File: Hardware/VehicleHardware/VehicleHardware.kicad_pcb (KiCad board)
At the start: 2 copper layers, 157.5 x 45.7 mm, 12 parts, among them U1 LM7805_TO220, U2 ESP32-CAM, U3 L298HN

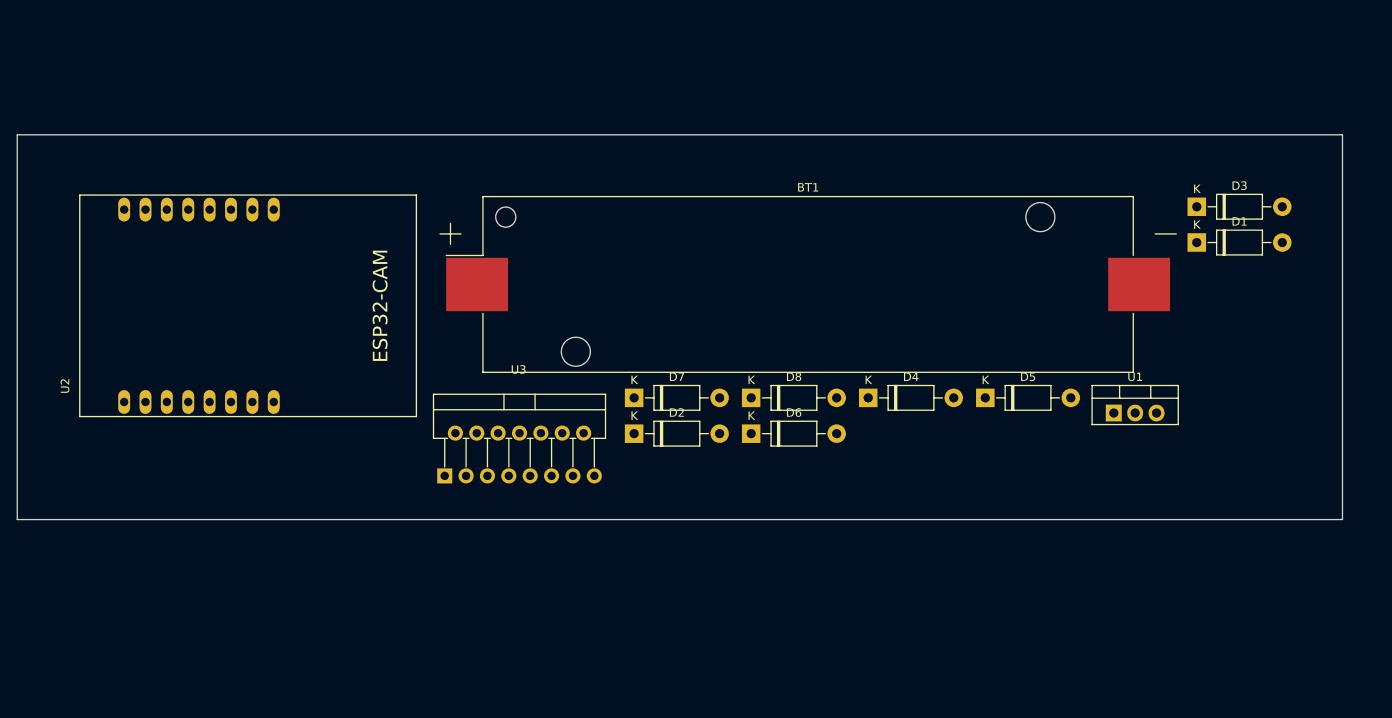
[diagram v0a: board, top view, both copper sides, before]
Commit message: added esp32-cam 3d-model; updated pcb design
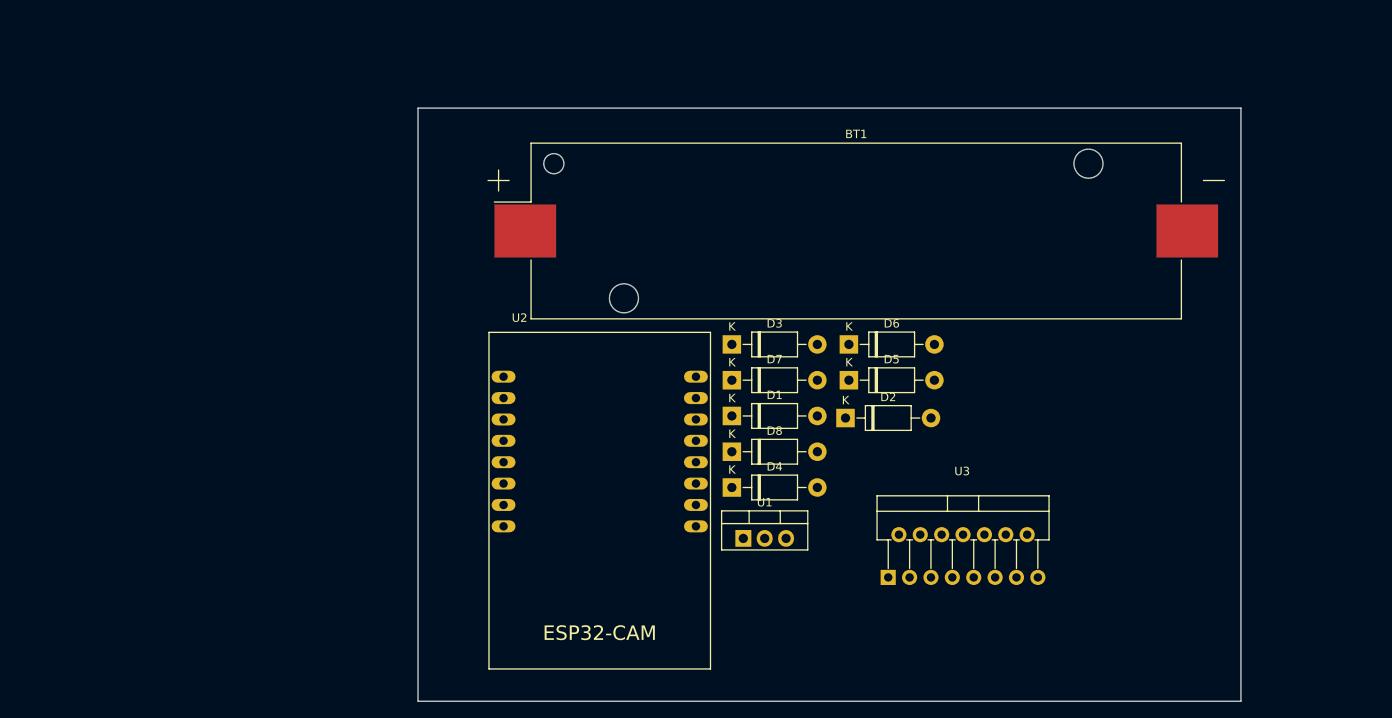
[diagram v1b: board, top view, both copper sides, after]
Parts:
- moved D1 59.0 mm to (128.1, 91.8)
- moved D3 57.6 mm to (128.1, 83.3)
- moved U3 54.1 mm to (155.5, 108.0)
- moved U2 49.9 mm to (112.4, 97.3), turned to 0 degrees
- moved U1 46.5 mm to (129.5, 106.4)
- moved D2 25.2 mm to (141.6, 92.1)
- moved D4 19.4 mm to (128.1, 100.3)
- moved D5 16.3 mm to (142.0, 87.6)
- moved D6 15.7 mm to (142.0, 83.3)
- moved D7 11.8 mm to (128.1, 87.6)
- moved BT1 8.54 mm to (142.9, 69.8)
- moved D8 6.80 mm to (128.1, 96.1)
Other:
- board size 157.5 x 45.7 mm -> 97.8 x 70.5 mm

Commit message: updated pcb and schematic;added header connectors;did some routing
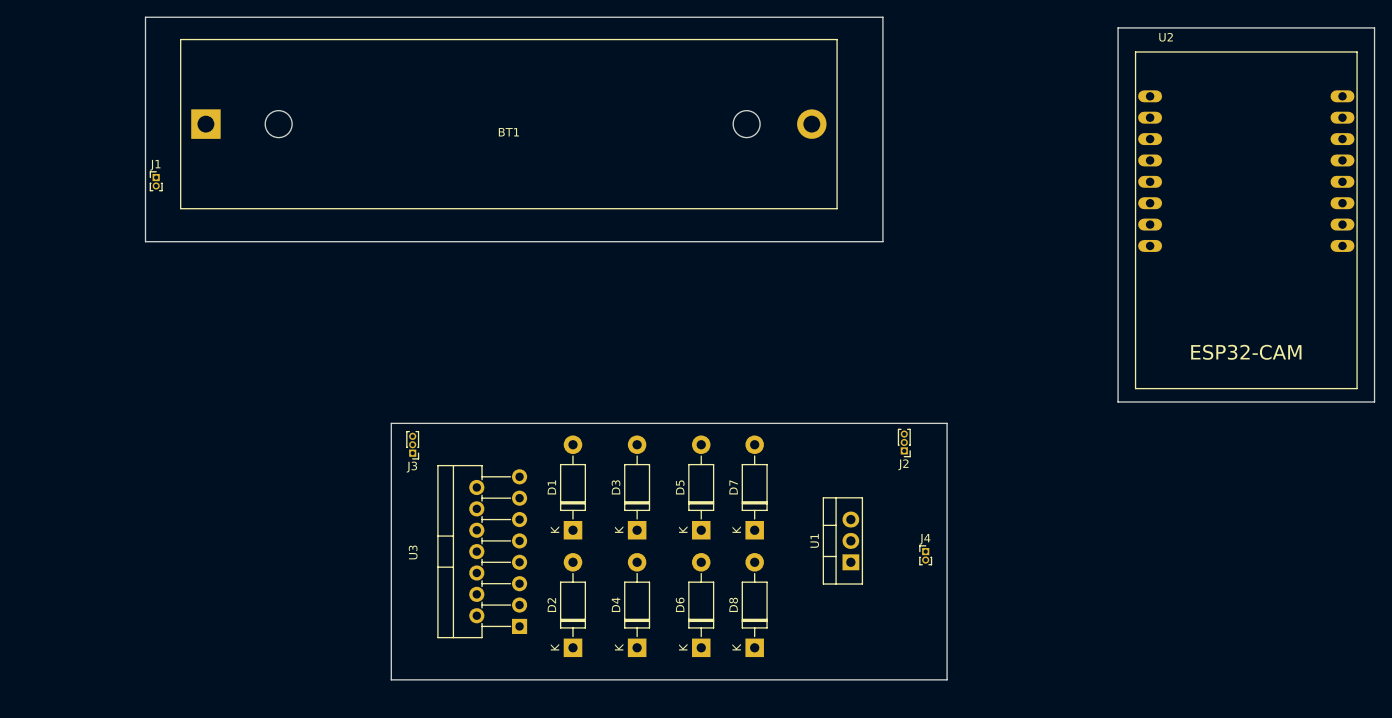
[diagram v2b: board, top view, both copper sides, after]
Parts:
- added J1: Conn_01x02_Male, Connector_PinHeader_1.00mm:PinHeader_1x02_P1.00mm_Vertical, F.Cu at (59.7, 63.5)
- added J2: Conn_01x03_Male, Connector_PinHeader_1.00mm:PinHeader_1x03_P1.00mm_Vertical, F.Cu at (148.6, 96.0)
- added J3: Conn_01x03_Male, Connector_PinHeader_1.00mm:PinHeader_1x03_P1.00mm_Vertical, F.Cu at (90.2, 96.2)
- added J4: Conn_01x02_Male, Connector_PinHeader_1.00mm:PinHeader_1x02_P1.00mm_Vertical, F.Cu at (151.1, 108.0)
- BT1: footprint Battery:BatteryHolder_Keystone_1042_1x18650 -> Battery:BatteryHolder_MPD_BH-18650-PC2
- moved U2 83.7 mm to (189.2, 64.0)
- moved BT1 78.3 mm to (65.6, 57.1)
- moved U3 55.7 mm to (99.8, 108.1), turned to 90 degrees
- moved D2 42.4 mm to (109.2, 119.4), turned to 90 degrees
- moved D6 40.1 mm to (124.5, 119.4), turned to 90 degrees
- moved D5 25.0 mm to (124.5, 105.4), turned to 90 degrees
- moved D3 24.8 mm to (116.8, 105.4), turned to 90 degrees
- moved D8 23.5 mm to (130.8, 119.4), turned to 90 degrees
- moved D1 23.3 mm to (109.2, 105.4), turned to 90 degrees
- moved D4 22.1 mm to (116.8, 119.4), turned to 90 degrees
- moved D7 18.0 mm to (130.8, 105.4), turned to 90 degrees
- moved U1 13.1 mm to (142.2, 109.2), turned to 90 degrees
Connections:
- net Net-(D1-Pad2) renamed /OUT1
- net Net-(D3-Pad2) renamed /OUT2
- net Net-(D5-Pad2) renamed /OUT3
- net Net-(D7-Pad2) renamed /OUT4
- BT1 pad 2: GND -> Net-(BT1-Pad2)
- D1 pad 1: Net-(BT1-Pad1) -> Net-(D1-Pad1)
- D3 pad 1: Net-(BT1-Pad1) -> Net-(D1-Pad1)
- D5 pad 1: Net-(BT1-Pad1) -> Net-(D1-Pad1)
- D7 pad 1: Net-(BT1-Pad1) -> Net-(D1-Pad1)
- U1 pad 1: Net-(BT1-Pad1) -> unconnected-(U1-Pad1)
- U1 pad 3: Net-(U1-Pad3) -> Net-(J4-Pad1)
- U2 pad 1: Net-(U2-Pad1) -> unconnected-(U2-Pad1)
- U2 pad 2: Net-(U2-Pad2) -> unconnected-(U2-Pad2)
- U2 pad 3: Net-(U2-Pad3) -> unconnected-(U2-Pad3)
- U2 pad 4: Net-(U2-Pad4) -> unconnected-(U2-Pad4)
- U2 pad 5: Net-(U2-Pad5) -> unconnected-(U2-Pad5)
- U2 pad 6: Net-(U2-Pad6) -> unconnected-(U2-Pad6)
- U2 pad 7: GND -> unconnected-(U2-Pad7)
- U2 pad 8: Net-(U1-Pad3) -> unconnected-(U2-Pad8)
- U3 pad 10: Net-(U2-Pad3) -> Net-(J3-Pad1)
- U3 pad 11: Net-(U2-Pad6) -> Net-(J3-Pad3)
- U3 pad 12: Net-(U2-Pad4) -> Net-(J3-Pad2)
- U3 pad 4: Net-(BT1-Pad1) -> Net-(D1-Pad1)
- U3 pad 5: Net-(U2-Pad1) -> Net-(J2-Pad1)
- U3 pad 6: Net-(U2-Pad5) -> Net-(J2-Pad3)
- U3 pad 7: Net-(U2-Pad2) -> Net-(J2-Pad2)
- U3 pad 9: Net-(U1-Pad3) -> Net-(J4-Pad1)
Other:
- board size 97.8 x 70.5 mm -> 146.1 x 78.7 mm
